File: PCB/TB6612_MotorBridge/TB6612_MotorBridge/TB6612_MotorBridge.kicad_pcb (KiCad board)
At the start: 4 copper layers, 44 x 44 mm, 14 parts, among them J1 Conn_01x05, J2 Conn_01x05, J3 Screw_Terminal_01x02, J4 Conn_01x02, J5 Conn_01x02, U1 TB6612FNG, U2 DMG3415U-7

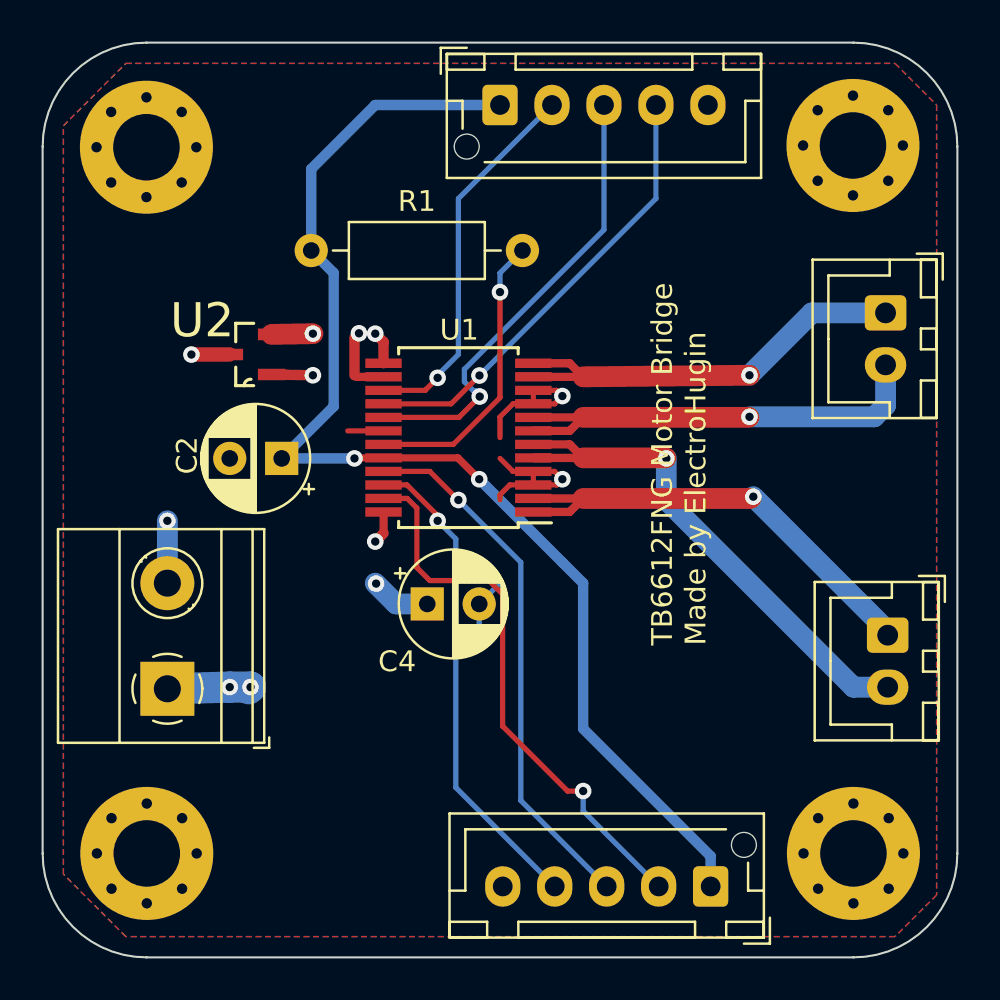
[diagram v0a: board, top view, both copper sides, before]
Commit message: Updated PCB Main and MotorBridge with Pins for Encoder
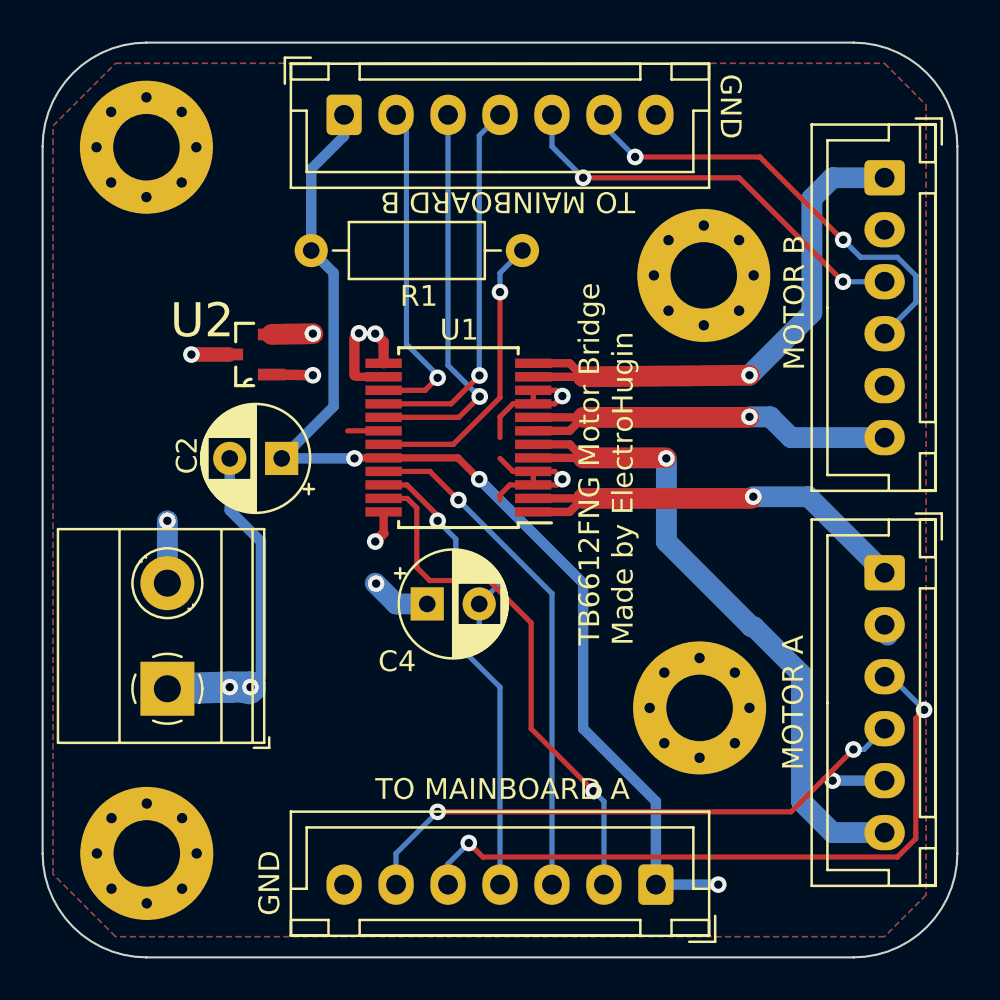
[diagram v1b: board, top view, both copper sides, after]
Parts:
- J1, J2: value Conn_01x05 -> Conn_01x07; footprint Connector_JST:JST_XH_B5B-XH-AM_1x05_P2.50mm_Vertical -> Connector_JST:JST_XH_B7B-XH-A_1x07_P2.50mm_Vertical
- J4, J5: value Conn_01x02 -> Conn_01x06; footprint Connector_JST:JST_XH_B2B-XH-A_1x02_P2.50mm_Vertical -> Connector_JST:JST_XH_B6B-XH-A_1x06_P2.50mm_Vertical
- moved H4 10.2 mm to (146.6, 99.0)
- moved H2 9.52 mm to (146.8, 78.2)
- moved J2 7.52 mm to (129.5, 70.5)
- moved J5 6.50 mm to (155.5, 73.5)
- moved J4 3.01 mm to (155.5, 92.5)
- moved J1 2.63 mm to (144.5, 107.5)
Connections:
- J1 pad 5: GND -> /EA1
- J2 pad 5: GND -> /EB1
- J4 pad 2: /MA2 -> GND
- J5 pad 2: /MB2 -> GND
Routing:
- net /EA1: track 0.00 -> 33.6 mm, vias 0 -> 2
- net /EA2: track 0.00 -> 27.5 mm, vias 0 -> 2
- net +3.3V: track 59.9 -> 85.6 mm, vias 2 -> 4
- net /EB2: track 0.00 -> 21.9 mm, vias 0 -> 2
- net /EB1: track 0.00 -> 20.2 mm, vias 0 -> 2
- net GND: track 25.5 -> 37.5 mm
- net /MA2: track 25.5 -> 33.0 mm
- net /MB1: track 21.0 -> 26.8 mm
- net /B2: track 21.7 -> 18.1 mm
- net /B1: track 22.3 -> 19.4 mm
- net /PWM_B: track 18.1 -> 16.2 mm
- net /MB2: track 21.8 -> 20.0 mm
- net /PWM_A: track 26.9 -> 25.3 mm
- net /MA1: track 22.7 -> 21.2 mm
- net /A2: track 23.4 -> 22.2 mm
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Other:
- board text added: "GND"
- board text added: "MOTOR A"
- board text added: "MOTOR B"
- board text added: "TO MAINBOARD A"
- board text added: "TO MAINBOARD B"
